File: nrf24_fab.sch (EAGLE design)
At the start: 23 parts, among them IC1 ATmega*8, IC2 MCP1702

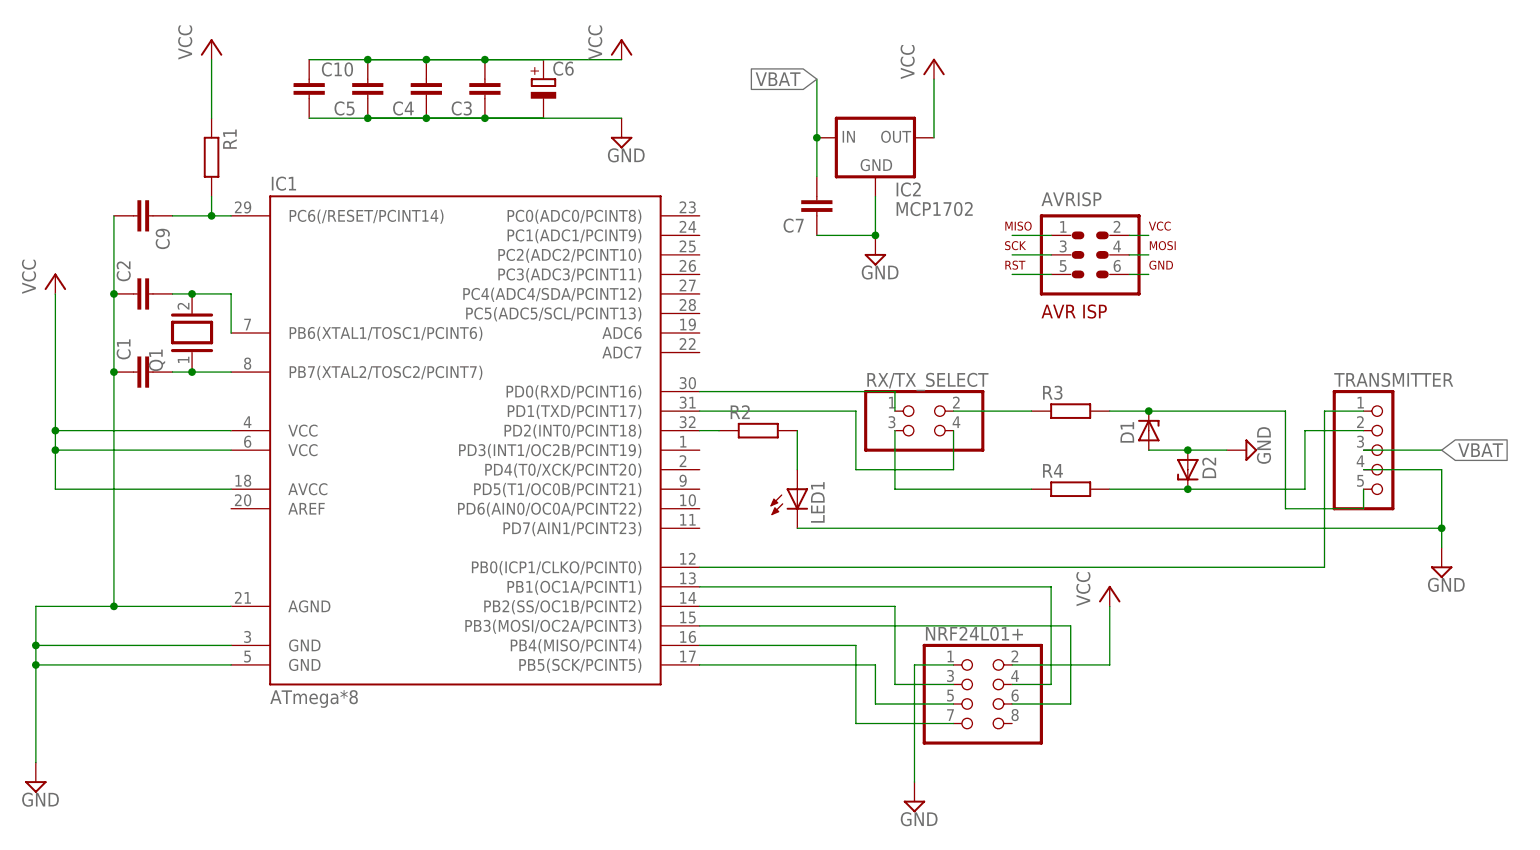
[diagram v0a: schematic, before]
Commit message: added parts values to schematic
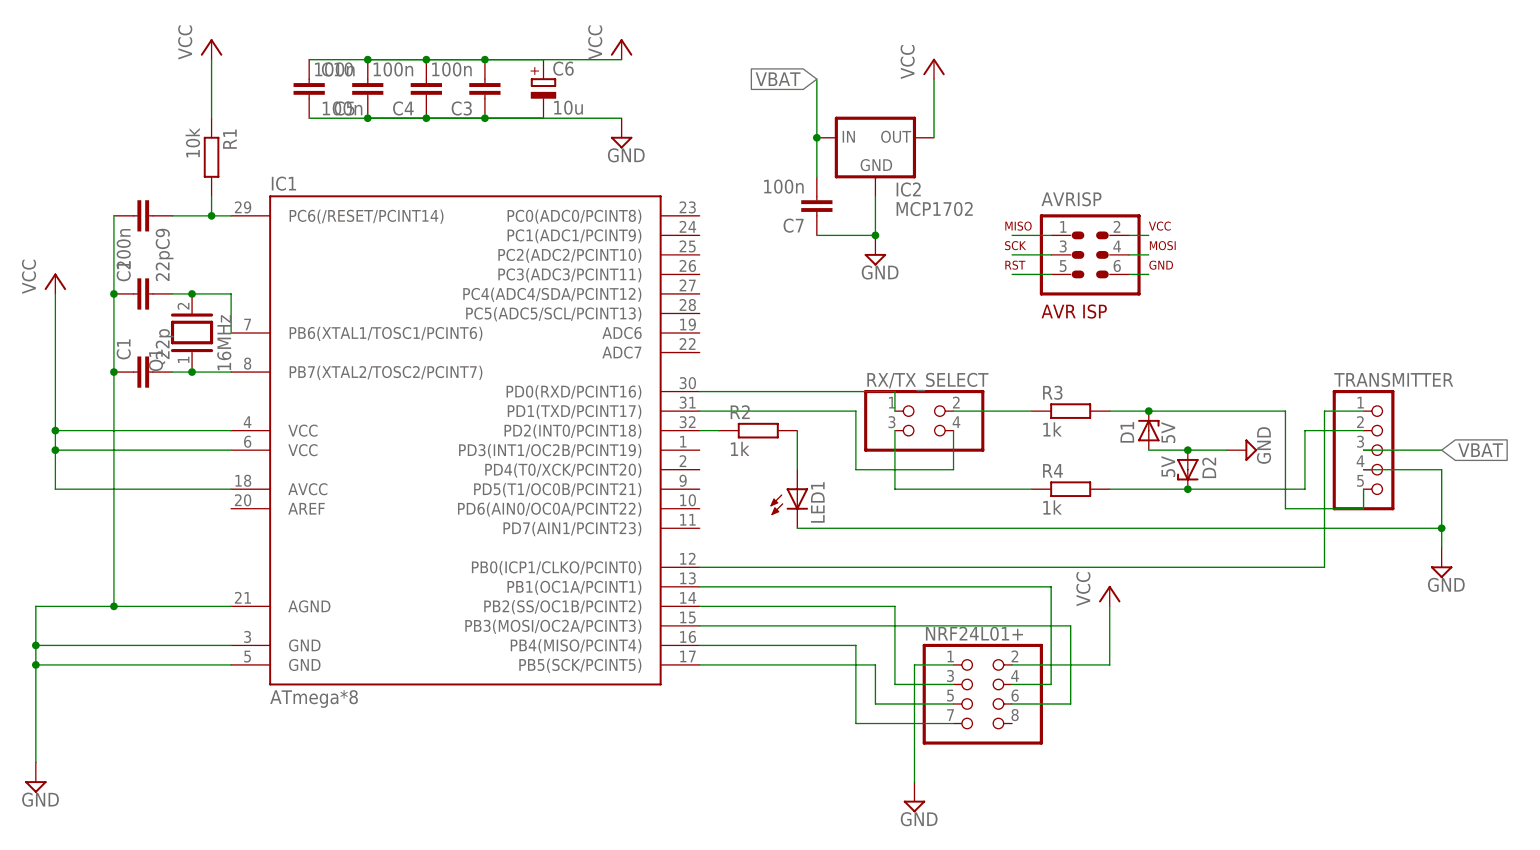
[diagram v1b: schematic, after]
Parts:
- C1, C2: value (none) -> 22p
- C10, C3, C4, C5, C7, C9: value (none) -> 100n
- C6: value (none) -> 10u
- D1, D2: value (none) -> 5V
- Q1: value (none) -> 16MHz
- R1: value (none) -> 10k
- R2, R3, R4: value (none) -> 1k
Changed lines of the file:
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@@
 <part name="P+5" library="supply1" deviceset="VCC" device=""/>
 <part name="SUPPLY5" library="supply2" deviceset="GND" device=""/>
-<part name="Q1" library="special" deviceset="XTAL/S" device=""/>
-<part name="C1" library="rcl" deviceset="C-EU" device="C0805"/>
-<part name="C2" library="rcl" deviceset="C-EU" device="C0805"/>
-<part name="C3" library="rcl" deviceset="C-EU" device="C0805"/>
-<part name="C4" library="rcl" deviceset="C-EU" device="C0805"/>
-<part name="C5" library="rcl" deviceset="C-EU" device="C0805"/>
-<part name="C6" library="rcl" deviceset="CPOL-EU" device="E2.5-6"/>
-<part name="C9" library="rcl" deviceset="C-EU" device="C0805"/>
+<part name="Q1" library="special" deviceset="XTAL/S" device="" value="16MHz"/>
+<part name="C1" library="rcl" deviceset="C-EU" device="C0805" value="22p"/>
+<part name="C2" library="rcl" deviceset="C-EU" device="C0805" value="22p"/>
+<part name="C3" library="rcl" deviceset="C-EU" device="C0805" value="100n"/>
+<part name="C4" library="rcl" deviceset="C-EU" device="C0805" value="100n"/>
+<part name="C5" library="rcl" deviceset="C-EU" device="C0805" value="100n"/>
+<part name="C6" library="rcl" deviceset="CPOL-EU" device="E2.5-6" value="10u"/>
+<part name="C9" library="rcl" deviceset="C-EU" device="C0805" value="100n"/>
 <part name="AVRISP" library="avr-7" deviceset="AVR-ISP-6" device="VERT"/>
-<part name="C10" library="rcl" deviceset="C-EU" device="C0805"/>
-<part name="R1" library="rcl" deviceset="R-EU_" device="M0805"/>
-<part name="R2" library="rcl" deviceset="R-EU_" device="M0805"/>
+<part name="C10" library="rcl" deviceset="C-EU" device="C0805" value="100n"/>
+<part name="R1" library="rcl" deviceset="R-EU_" device="M0805" value="10k"/>
+<part name="R2" library="rcl" deviceset="R-EU_" device="M0805" value="1k"/>
 <part name="LED1" library="led" deviceset="LED" device="SMT1206"/>
 <part name="IC2" library="Alis custom parts" deviceset="MCP1702" device=""/>
 <part name="P+4" library="supply1" deviceset="VCC" device=""/>
-<part name="C7" library="rcl" deviceset="C-EU" device="C0805"/>
-<part name="R3" library="rcl" deviceset="R-EU_" device="M0805"/>
-<part name="R4" library="rcl" deviceset="R-EU_" device="M0805"/>
-<part name="D1" library="diode" deviceset="ZENER-DIODE" device="SOD80C"/>
-<part name="D2" library="diode" deviceset="ZENER-DIODE" device="SOD80C"/>
+<part name="C7" library="rcl" deviceset="C-EU" device="C0805" value="100n"/>
+<part name="R3" library="rcl" deviceset="R-EU_" device="M0805" value="1k"/>
+<part name="R4" library="rcl" deviceset="R-EU_" device="M0805" value="1k"/>
+<part name="D1" library="diode" deviceset="ZENER-DIODE" device="SOD80C" value="5V"/>
+<part name="D2" library="diode" deviceset="ZENER-DIODE" device="SOD80C" value="5V"/>
 <part name="SUPPLY6" library="supply2" deviceset="GND" device=""/>
 </parts>
